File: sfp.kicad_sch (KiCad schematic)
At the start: 157 parts, among them J6 SFP+x8, U1 74LVC8T245, U2 74LVC8T245, U3 TCA9546A, U4 TCA9546A

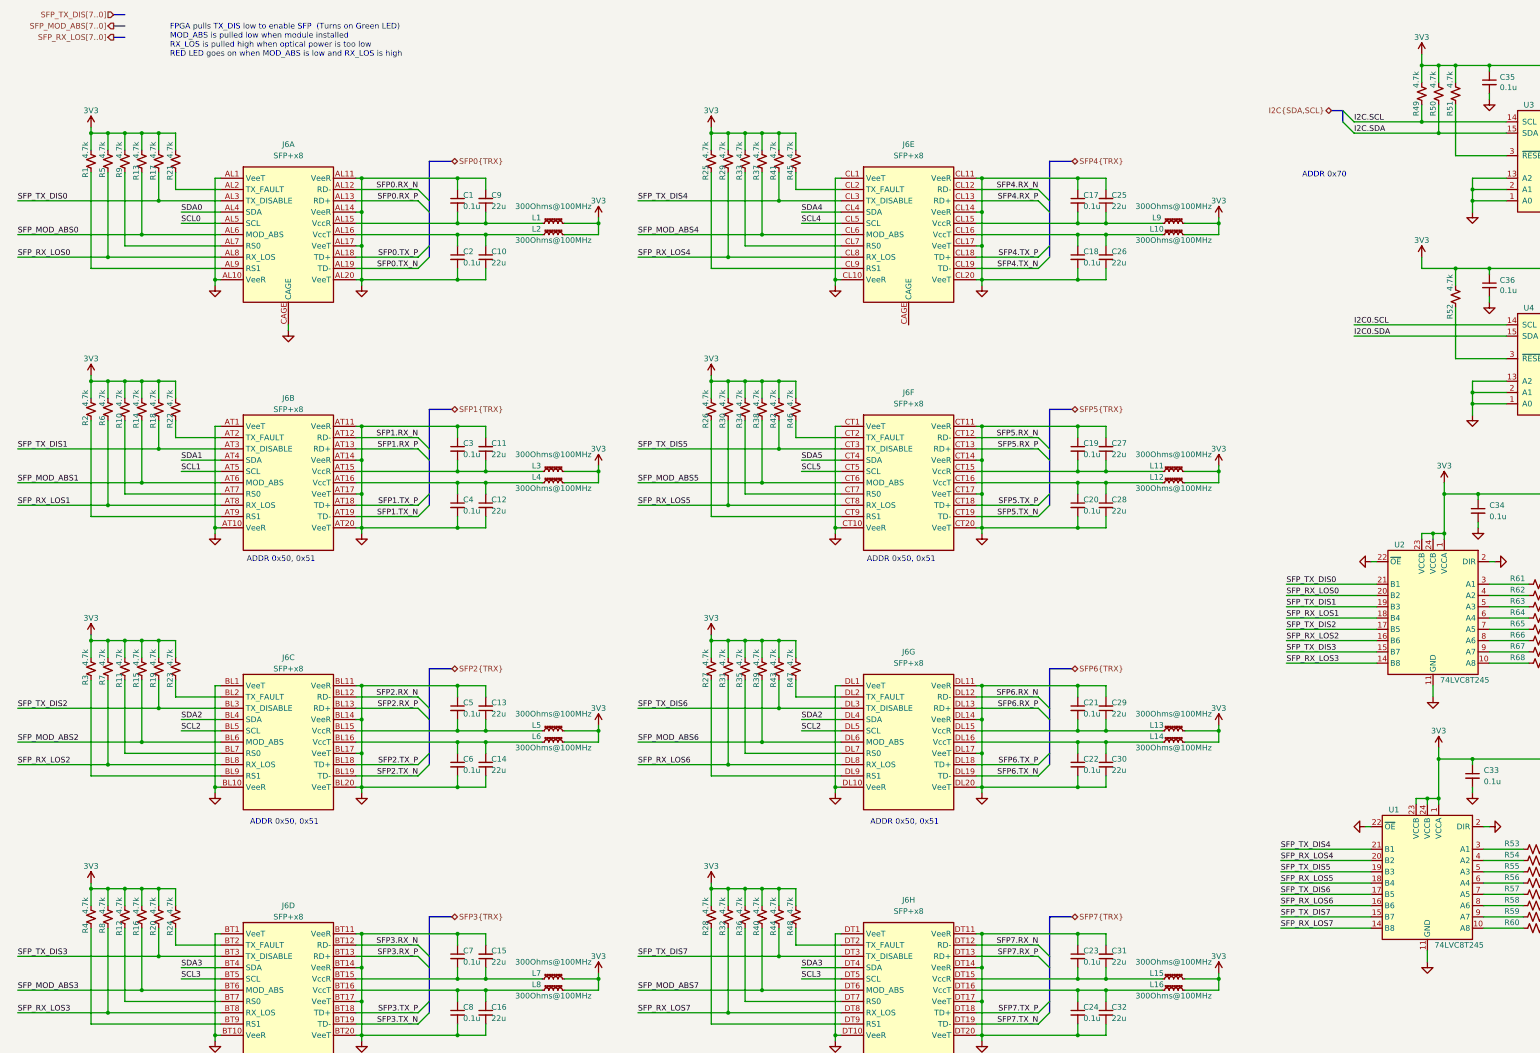
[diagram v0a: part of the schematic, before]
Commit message: Start routing SFP
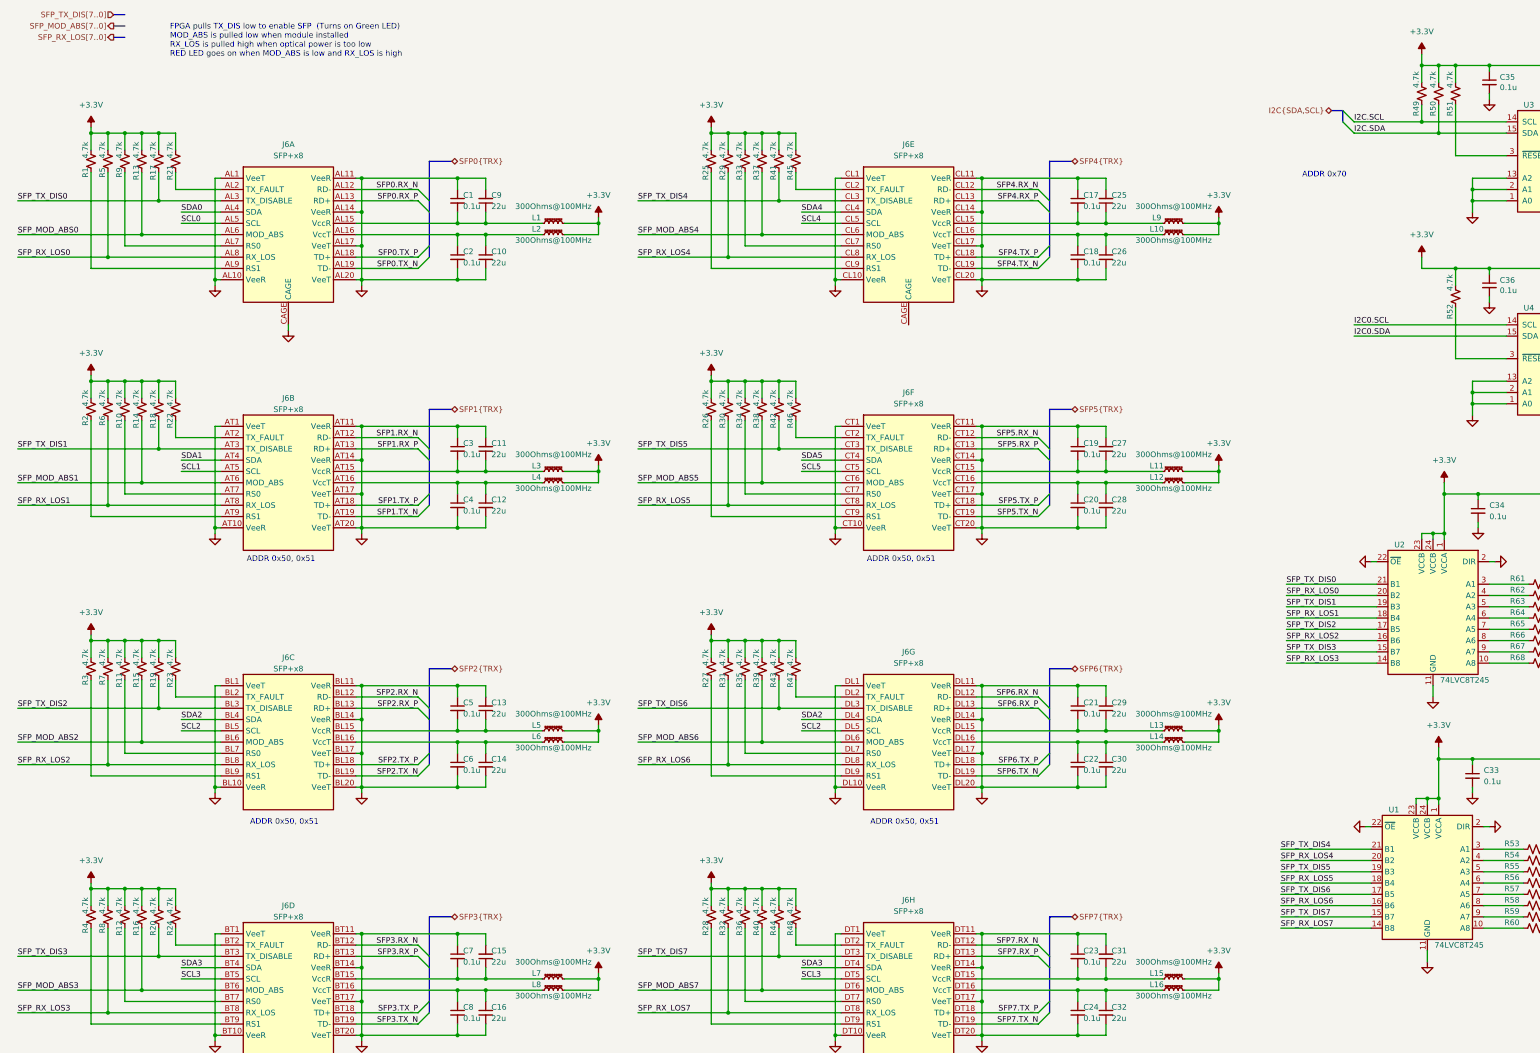
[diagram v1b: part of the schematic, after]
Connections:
- net 3V3 renamed +3.3V

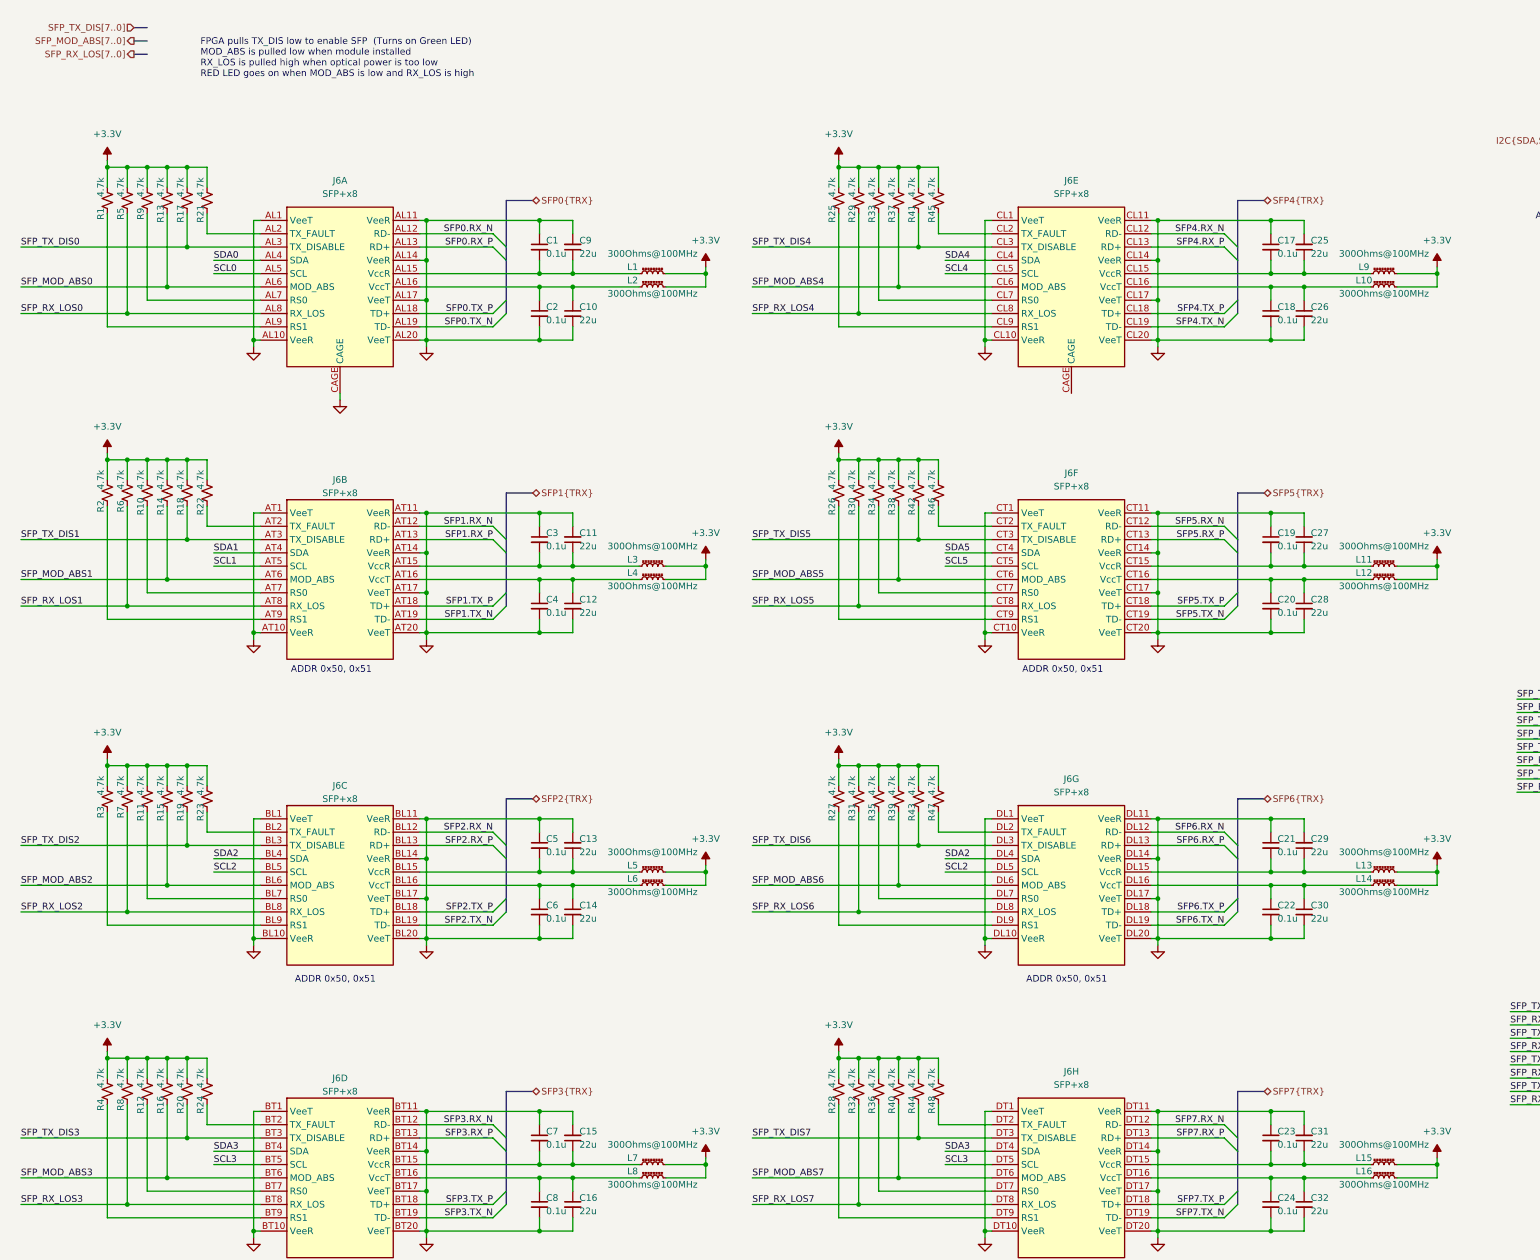
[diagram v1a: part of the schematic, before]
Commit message: Start routing diff pairs
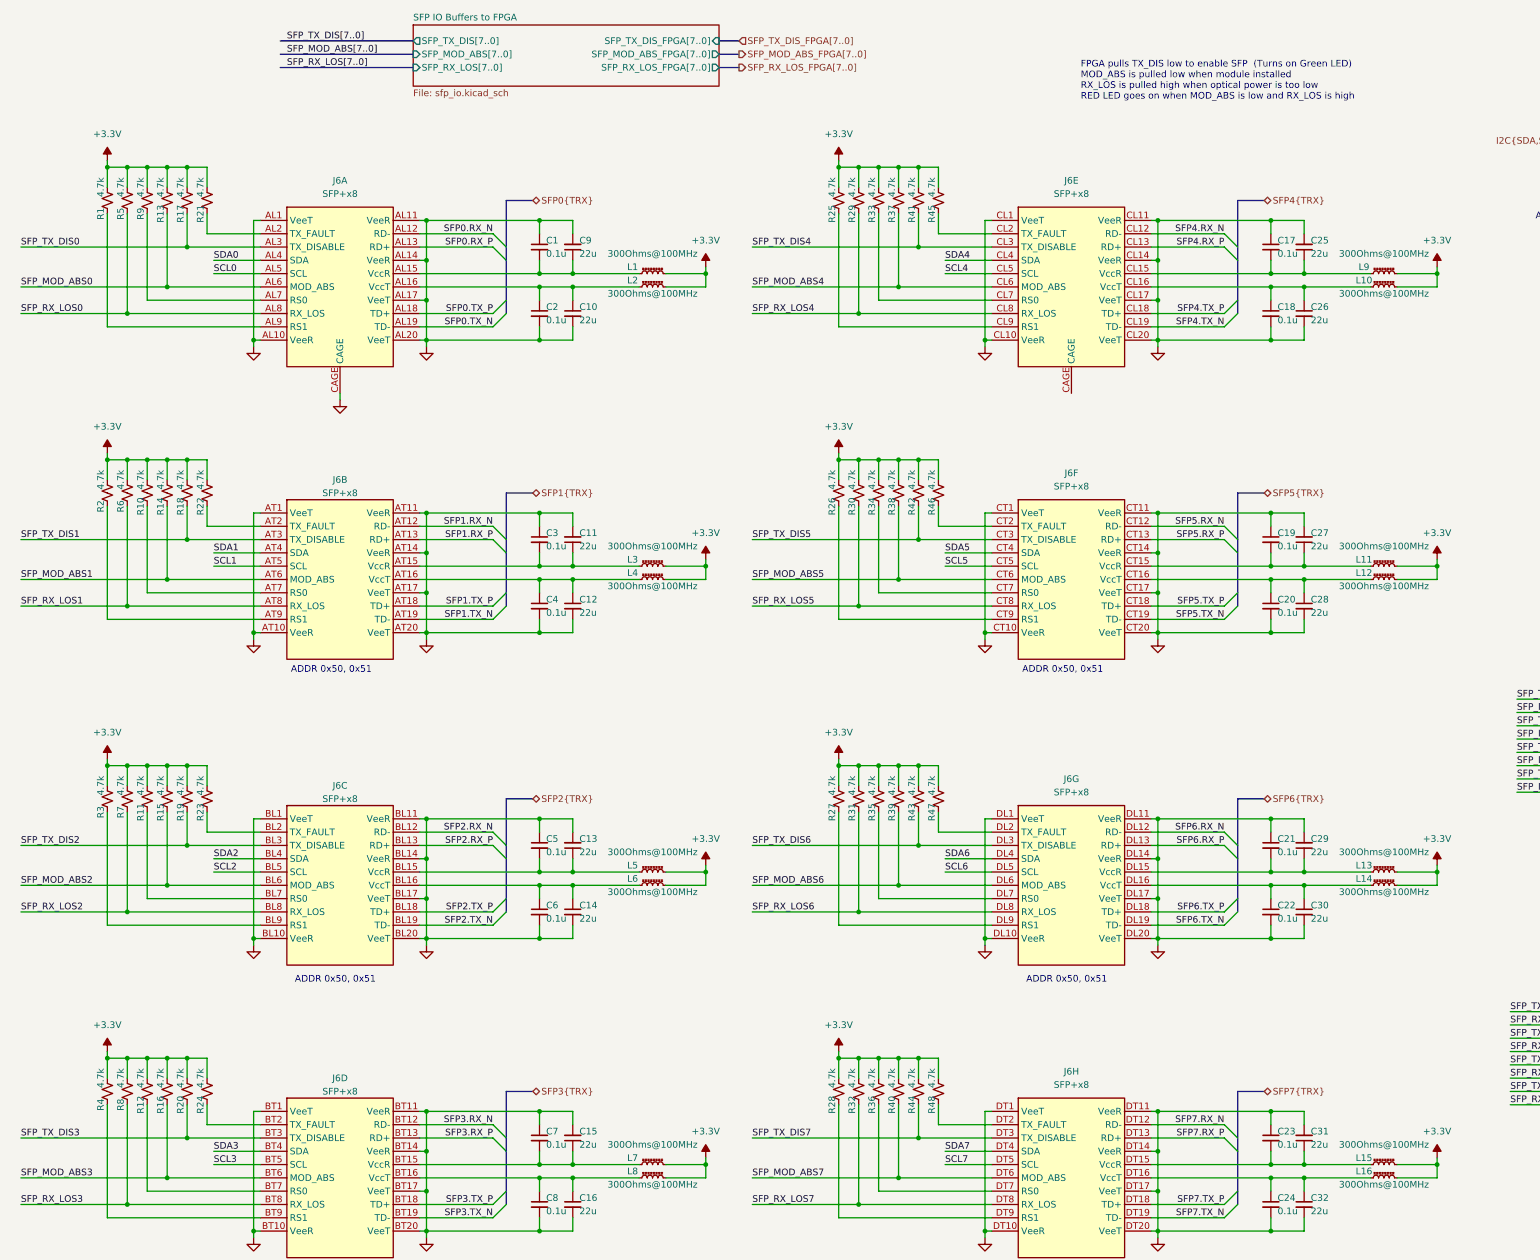
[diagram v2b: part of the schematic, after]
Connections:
- net SCL2: no longer J6.DL5 (SCL)
- net SCL3: no longer J6.DT5 (SCL)
- net SCL6: now also J6.DL5 (SCL)
- net SCL7: now also J6.DT5 (SCL)
- net SDA2: no longer J6.DL4 (SDA)
- net SDA3: no longer J6.DT4 (SDA)
- net SDA6: now also J6.DL4 (SDA)
- net SDA7: now also J6.DT4 (SDA)
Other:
- added sheet SFP IO Buffers to FPGA (sfp_io.kicad_sch)
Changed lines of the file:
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@@
 	(text "FPGA pulls TX_DIS low to enable SFP  (Turns on Green LED)\nMOD_ABS is pulled low when module installed\nRX_LOS is pulled high when optical power is too low\nRED LED goes on when MOD_ABS is low and RX_LOS is high"
 		(exclude_from_sim no)
-		(at 50.8 26.162 0)
+		(at 218.948 30.48 0)
 		(effects
 			(font
@@
 		)
 	)
-	(bus
-		(pts
-			(xy 38.1 20.32) (xy 40.64 20.32)
-		)
-		(stroke
-			(width 0)
-			(type default)
-		)
-	)
 	(wire
 		(pts
@@
 	(bus
 		(pts
+			(xy 149.86 25.4) (xy 153.67 25.4)
+		)
+		(stroke
+			(width 0)
+			(type default)
+		)
+	)
+	(bus
+		(pts
 			(xy 109.22 232.41) (xy 109.22 223.52)
 		)
@@
 		)
 	)
+	(bus
+		(pts
+			(xy 149.86 27.94) (xy 153.67 27.94)
+		)
+		(stroke
+			(width 0)
+			(type default)
+		)
+	)
 	(wire
 		(pts
@@
 		)
 	)
+	(bus
+		(pts
+			(xy 66.04 22.86) (xy 91.44 22.86)
+		)
+		(stroke
+			(width 0)
+			(type default)
+		)
+	)
 	(wire
 		(pts
@@
 		)
 	)
-	(bus
-		(pts
-			(xy 38.1 22.86) (xy 40.64 22.86)
-		)
-		(stroke
-			(width 0)
-			(type default)
-		)
-	)
 	(wire
 		(pts
@@
 		)
 	)
+	(bus
+		(pts
+			(xy 66.04 25.4) (xy 91.44 25.4)
+		)
+		(stroke
+			(width 0)
+			(type default)
+		)
+	)
 	(wire
 		(pts
@@
 	(bus
 		(pts
+			(xy 149.86 22.86) (xy 153.67 22.86)
+		)
+		(stroke
+			(width 0)
+			(type default)
+		)
+	)
+	(bus
+		(pts
 			(xy 248.92 232.41) (xy 248.92 223.52)
 		)
@@
 		)
 	)
-	(bus
-		(pts
-			(xy 38.1 25.4) (xy 40.64 25.4)
-		)
-		(stroke
-			(width 0)
-			(type default)
-		)
-	)
 	(wire
 		(pts
@@
 		)
 	)
+	(bus
+		(pts
+			(xy 66.04 27.94) (xy 91.44 27.94)
+		)
+		(stroke
+			(width 0)
+			(type default)
+		)
+	)
 	(wire
 		(pts
@@
 		)
 	)
-	(label "SDA3"
+	(label "SDA7"
 		(at 193.04 234.95 0)
 		(effects
@@
 		)
 	)
-	(label "SCL3"
+	(label "SCL7"
 		(at 193.04 237.49 0)
 		(effects
@@
 		)
 	)
-	(label "SDA2"
+	(label "SDA6"
 		(at 193.04 179.07 0)
 		(effects
@@
 		)
 	)
-	(label "SCL2"
+	(label "SCL6"
 		(at 193.04 181.61 0)
 		(effects
@@
 		)
 	)
+	(label "SFP_TX_DIS[7..0]"
+		(at 67.31 22.86 0)
+		(effects
+			(font
+				(size 1.27 1.27)
+			)
+			(justify left bottom)
+		)
+	)
 	(label "SFP_MOD_ABS1"
 		(at 412.75 156.21 180)
@@
 		)
 	)
+	(label "SFP_RX_LOS[7..0]"
+		(at 67.31 27.94 0)
+		(effects
+			(font
+				(size 1.27 1.27)
+			)
+			(justify left bottom)
+		)
+	)
 	(label "SFP_MOD_ABS7"
 		(at 156.21 240.03 0)
@@
 		)
 	)
+	(label "SFP_MOD_ABS[7..0]"
+		(at 67.31 25.4 0)
+		(effects
+			(font
+				(size 1.27 1.27)
+			)
+			(justify left bottom)
+		)
+	)
 	(label "SFP2.TX_N"
 		(at 106.68 191.77 180)
@@
 		)
 	)
-	(hierarchical_label "SFP_TX_DIS[7..0]"
-		(shape input)
-		(at 38.1 20.32 180)
+	(hierarchical_label "SFP_RX_LOS_FPGA[7..0]"
+		(shape output)
+		(at 153.67 27.94 0)
 		(effects
 			(font
 				(size 1.27 1.27)
 			)
-			(justify right)
+			(justify left)
 		)
 	)
@@
 		)
 	)
+	(hierarchical_label "SFP_TX_DIS_FPGA[7..0]"
+		(shape input)
+		(at 153.67 22.86 0)
+		(effects
+			(font
+				(size 1.27 1.27)
+			)
+			(justify left)
+		)
+	)
 	(hierarchical_label "I2C{SDA,SCL}"
 		(shape bidirectional)
@@
 		)
 	)
+	(hierarchical_label "SFP_MOD_ABS_FPGA[7..0]"
+		(shape output)
+		(at 153.67 25.4 0)
+		(effects
+			(font
+				(size 1.27 1.27)
+			)
+			(justify left)
+		)
+	)
 	(hierarchical_label "SFP4{TRX}"
 		(shape bidirectional)
@@
 		)
 	)
-	(hierarchical_label "SFP_MOD_ABS[7..0]"
-		(shape output)
-		(at 38.1 22.86 180)
-		(effects
-			(font
-				(size 1.27 1.27)
-			)
-			(justify right)
-		)
-	)
-	(hierarchical_label "SFP_RX_LOS[7..0]"
-		(shape output)
-		(at 38.1 25.4 180)
-		(effects
-			(font
-				(size 1.27 1.27)
-			)
-			(justify right)
-		)
-	)
 	(hierarchical_label "SFP1{TRX}"
 		(shape bidirectional)
@@
 				)
 			)
+		)
+	)
+	(sheet
+		(at 91.44 19.812)
+		(size 58.42 11.684)
+		(exclude_from_sim no)
+		(in_bom yes)
+		(on_board yes)
+		(dnp no)
+		(fields_autoplaced yes)
+		(stroke
+			(width 0.1524)
+			(type solid)
+		)
+		(fill
+			(color 255 255 194 1.0000)
+		)
+		(property "Sheetname" "SFP IO Buffers to FPGA"
+			(at 91.44 19.1004 0)
+			(effects
+				(font
+					(size 1.27 1.27)
+				)
+				(justify left bottom)
+			)
+		)
+		(property "Sheetfile" "sfp_io.kicad_sch"
+			(at 91.44 32.0806 0)
+			(effects
+				(font
+					(size 1.27 1.27)
+				)
+				(justify left top)
+			)
+		)
+		(pin "SFP_MOD_ABS[7..0]" input
+			(at 91.44 25.4 180)
+			(effects
+				(font
+					(size 1.27 1.27)
+				)
+				(justify left)
+			)
+		)
+		(pin "SFP_MOD_ABS_FPGA[7..0]" output
+			(at 149.86 25.4 0)
+			(effects
+				(font
+					(size 1.27 1.27)
+				)
+				(justify right)
+			)
+		)
+		(pin "SFP_RX_LOS[7..0]" input
+			(at 91.44 27.94 180)
+			(effects
+				(font
+					(size 1.27 1.27)
+				)
+				(justify left)
+			)
+		)
+		(pin "SFP_RX_LOS_FPGA[7..0]" output
+			(at 149.86 27.94 0)
+			(effects
+				(font
+					(size 1.27 1.27)
+				)
+				(justify right)
+			)
+		)
+		(pin "SFP_TX_DIS[7..0]" output
+			(at 91.44 22.86 180)
+			(effects
+				(font
+					(size 1.27 1.27)
+				)
+				(justify left)
+			)
+		)
+		(pin "SFP_TX_DIS_FPGA[7..0]" input
+			(at 149.86 22.86 0)
+			(effects
+				(font
+					(size 1.27 1.27)
+				)
+				(justify right)
+			)
+		)
+		(instances
+			(project "cc-afe"
+				(path "/40891cc8-bf64-41f4-8f69-a607d7b280eb/3f2dcaf9-8852-4ae9-a02f-0828e41c6a78"
+					(page "9")
+				)
+			)

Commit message: Finish board, sent out for quote
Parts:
- added C114, C115: 0.1u, Capacitor_SMD:C_0603_1608Metric, symbol Device:C_Small
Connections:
- net +3.3V: now also C114.1, C115.1
- net GND: now also C114.2, C115.2
